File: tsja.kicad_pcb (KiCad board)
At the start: 4 copper layers, 95 x 86 mm, 117 parts, among them J1 QWIIC, J10 E-Paper, J2 Micro_SD_Card, J3 SAO, J4 EXT, J6 USB-C, J9 Battery, M1 Vibration, Q1 AP2302B, Q2 AP2302B, Q3 AP2302B, Q4 AO3400 (A09T), Q5 AO3400 (A09T), SW6 SW_SPDT, T1 Select, T2 Start, T3 B, T4 A, T5 Cross, U1 74LVC1G17GW,125, U10 SY6280AAC, U11 SK6805, U12 SK6805, U13 SK6805, U14 SK6805, U15 SK6805, U2 MPR121QR2, U3 ESP32-WROVER-E, U4 TPS63020DSJR, U5 XT4054K421MR-G, U6 SY6280AAC, U7 CH340K, U8 SK6805, U9 SY6280AAC

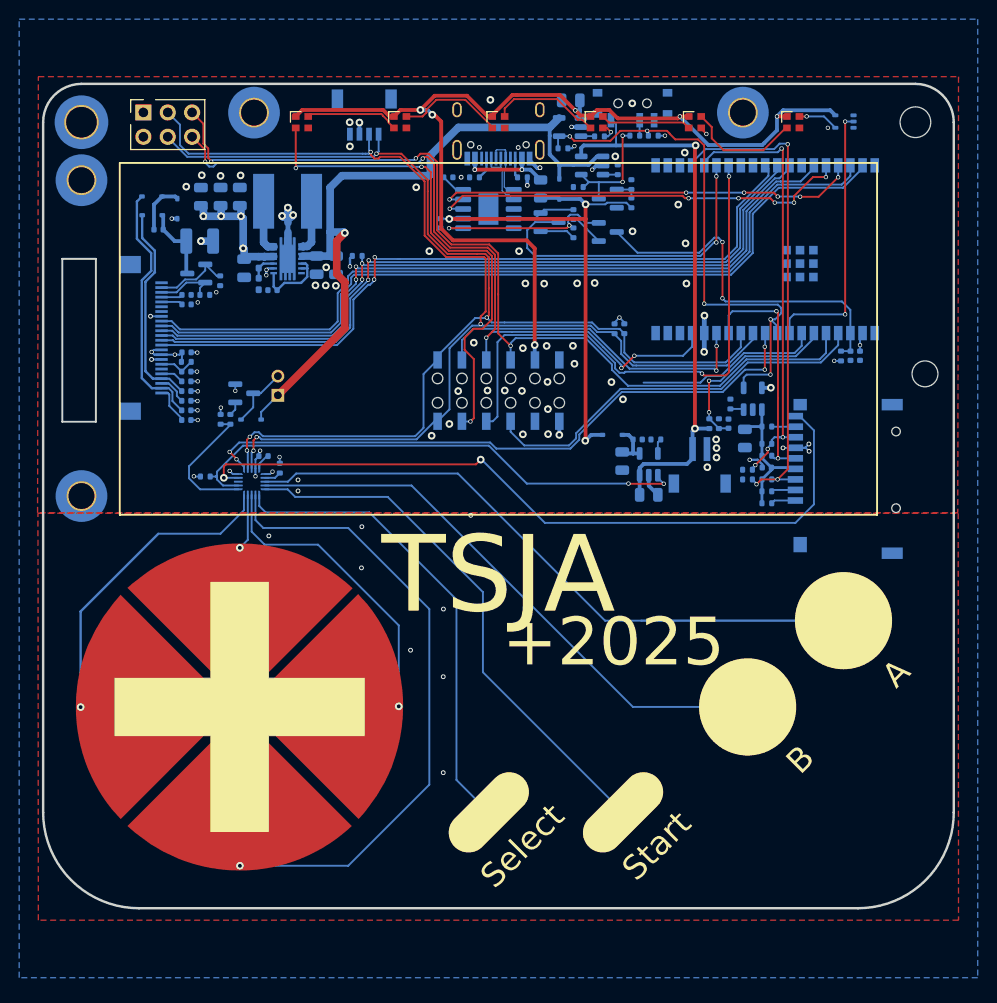
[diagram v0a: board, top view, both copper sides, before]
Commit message: No DRC errors
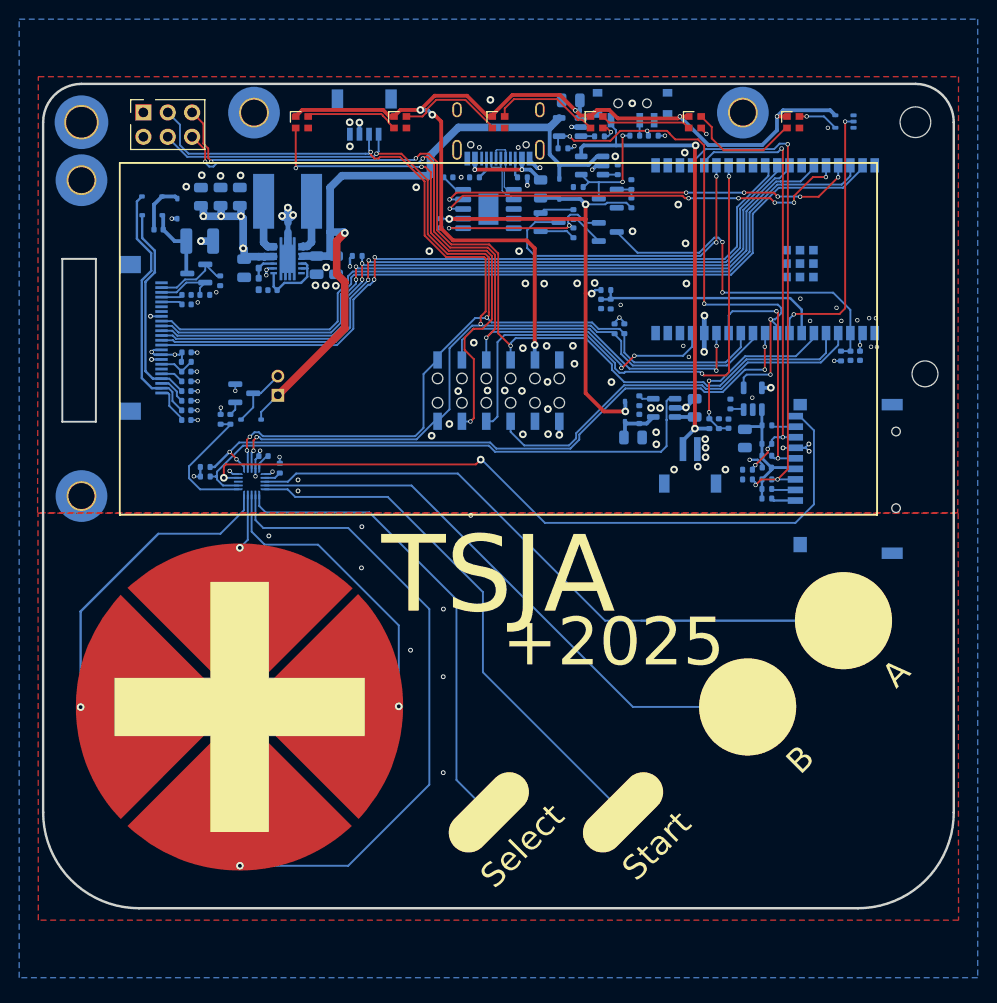
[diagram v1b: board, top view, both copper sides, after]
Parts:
- added C30: 100n, Capacitor_SMD:C_0402_1005Metric, B.Cu at (10.7, -20.3)
- added R23: 100k, Resistor_SMD:R_0402_1005Metric, B.Cu at (11.2, -21.7)
- added R24: 100k, Resistor_SMD:R_0402_1005Metric, B.Cu at (11.7, -20.3)
- added R40: 10k, Resistor_SMD:R_0402_1005Metric, B.Cu at (-30.6, -3.28)
- SW6: footprint Button_Switch_SMD:SW_SPDT_PCM12 -> library:SW_SPDT_PCM12_MP
- moved C11 10.3 mm to (20.5, -9.45), turned to 90 degrees
- moved U5 6.11 mm to (17.3, -9.45), turned to 180 degrees
- moved R25 4.39 mm to (14.7, -10.2), turned to 90 degrees
- moved D23 2.75 mm to (13.2, -9.05), turned to 90 degrees
- moved C6 2.71 mm to (14.0, -6.36), turned to 180 degrees
- moved C8 2.15 mm to (14.7, -8.29), turned to -90 degrees
- moved J9 1.00 mm to (20.0, -3.00)
- moved R17 0.49 mm to (28.0, 0.01)
- moved R18 0.25 mm to (28.0, -0.99)
- moved R22 0.12 mm to (28.0, -7.62)
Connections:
- net VBAT_SENSE renamed VBATT_SENSE
- U3 pad 7: unconnected-(U3-GPIO35/ADC1_CH7-Pad7) -> VBUS_SENSE
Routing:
- net VBUS_SENSE: track 0.00 -> 24.7 mm
- net unconnected-(U3-GPIO35/ADC1_CH7-Pad7): track 19.4 -> 0.00 mm
- net VBATT: track 59.1 -> 52.4 mm
- net CHRG: track 54.5 -> 58.3 mm, vias 2 -> 0
- net TOUCH_INT: track 66.4 -> 69.2 mm
- net VSDCARD: track 15.0 -> 13.9 mm
- net VBUS: track 53.4 -> 54.1 mm, vias 3 -> 4
- net Net-(U7-V3): track 2.57 -> 1.85 mm
- net EP_DATA: track 77.8 -> 77.1 mm
- net Net-(SW6-B): track 1.95 -> 1.27 mm
- net /USB_P: track 6.88 -> 6.20 mm
- net EP_SCK: track 77.9 -> 77.2 mm
- net SD_DET: track 78.6 -> 78.0 mm
- net VBATT_SENSE: track 19.7 -> 19.1 mm
- net I2C_SDA: track 121.8 -> 121.2 mm
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
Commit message: Cleanup & tweaks
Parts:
- added N1: Board, design:board, F.Cu at (0.00, 0.00)
- M1: footprint Connector_PinHeader_2.00mm:PinHeader_1x02_P2.00mm_Vertical -> Connector_PinHeader_2.54mm:PinHeader_1x02_P2.54mm_Vertical_SMD_Pin1Left
- moved M1 2.17 mm to (-21.0, -11.7), turned to 180 degrees
- moved J9 2.00 mm to (20.0, -1.00), turned to 90 degrees
- moved C27 0.65 mm to (7.54, -40.9)
- moved H3 0.65 mm to (-43.5, -32.5)
- moved U1 0.65 mm to (36.1, -38.7)
- moved C13 0.65 mm to (-35.5, -27.4)
- moved C17 0.65 mm to (-32.5, -20.6)
- moved C29 0.65 mm to (-23.6, -21.1)
- moved C3 0.65 mm to (-6.05, -28.1)
- moved C9 0.65 mm to (-31.0, -30.8)
- moved D24 0.65 mm to (6.35, -31.6)
- moved D25 0.65 mm to (-33.5, -29.6)
- moved D26 0.65 mm to (-36.1, -30.9)
- moved D27 0.65 mm to (-36.1, -28.9)
- moved Q5 0.65 mm to (5.34, -28.2)
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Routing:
- net SD_DET: track 78.0 -> 64.4 mm
- net VBATT: track 52.4 -> 55.9 mm
- net VIN: track 74.9 -> 78.4 mm, vias 1 -> 4
- net GND: track 39.1 -> 37.9 mm, vias 116 -> 124
